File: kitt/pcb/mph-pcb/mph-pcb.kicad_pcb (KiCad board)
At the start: 4 copper layers, 280 x 125 mm, 140 parts, among them J1 Screw_Terminal_01x02, J2 Screw_Terminal_01x03, U1 TLC5940NT, U2 TLC5940NT, U3 TLC5940NT, U4 TLC5940NT, U5 TLC5940NT, U6 TLC5940NT, U7 TLC5940NT

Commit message: routed led display chips
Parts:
- moved C4 232.2 mm to (151.1, 136.2)
- moved NT7 213.6 mm to (231.5, 107.5)
- moved NT5 194.1 mm to (222.7, 39.1), turned to 180 degrees
- moved R3 194.0 mm to (74.2, 81.5), turned to 90 degrees
- moved C8 185.1 mm to (190.7, 110.8), turned to 180 degrees
- moved R4 184.9 mm to (136.4, 48.5), turned to 90 degrees
- moved NT6 170.6 mm to (188.3, 107.5)
- moved R7 164.1 mm to (226.1, 110.3), turned to 180 degrees
- moved C5 159.8 mm to (70.3, 81.5), turned to 90 degrees
- moved R34 159.1 mm to (66.0, 71.4), turned to 270 degrees
- moved C9 158.8 mm to (233.9, 110.1), turned to 180 degrees
- moved NT2 155.8 mm to (148.5, 132.4), turned to 270 degrees
- moved R2 150.0 mm to (159.9, 136.2)
- moved R6 143.7 mm to (182.9, 110.3), turned to 180 degrees
- moved C6 139.2 mm to (132.7, 49.1), turned to 90 degrees
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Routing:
- added copper zone on In2.Cu, net GND

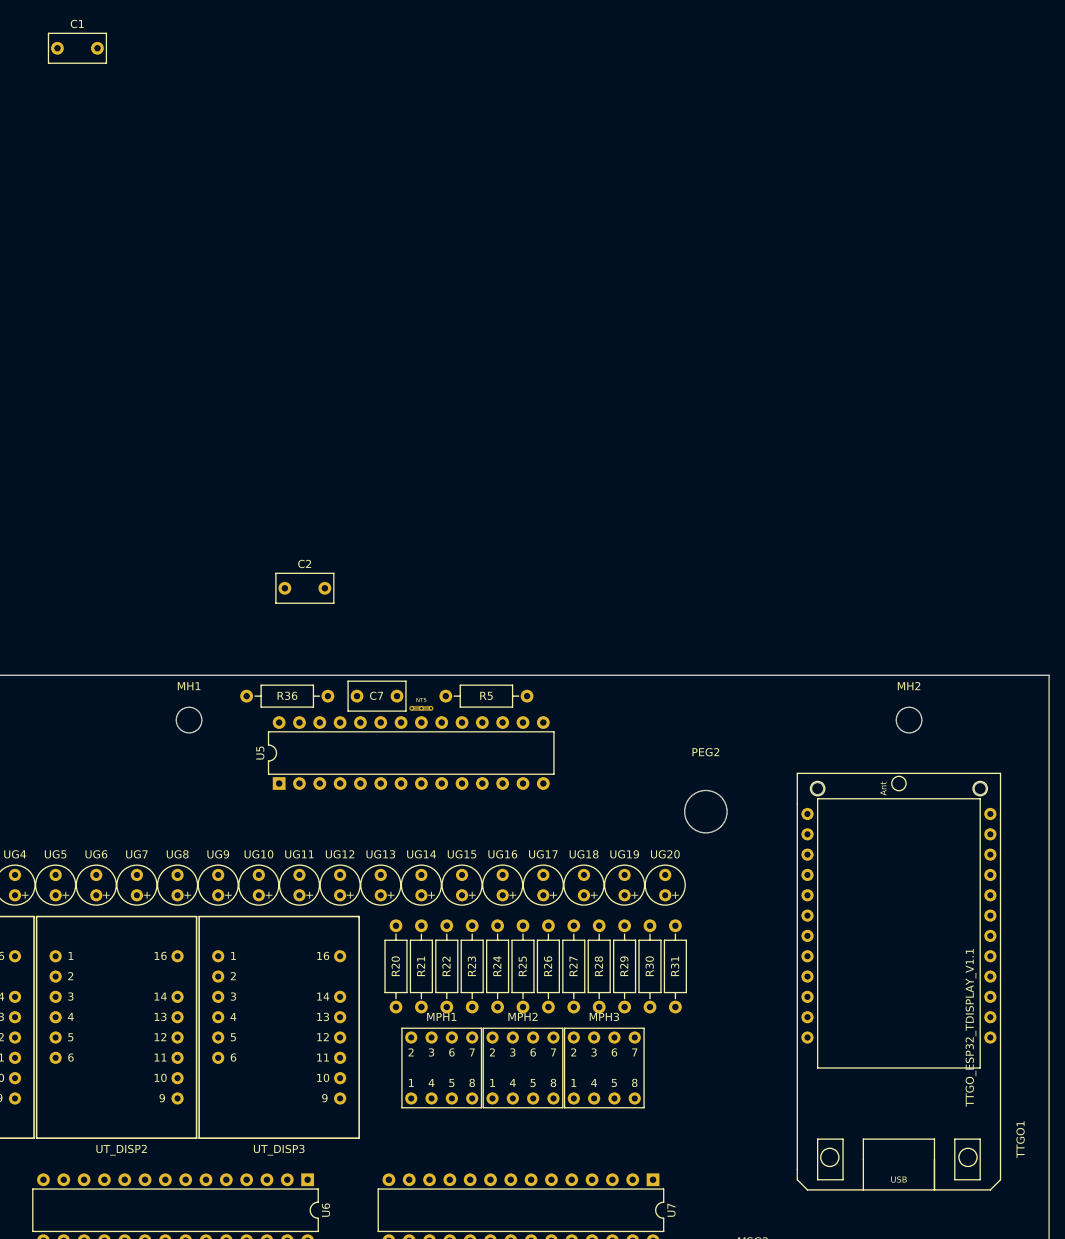
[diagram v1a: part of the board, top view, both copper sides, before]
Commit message: finshed mph placement
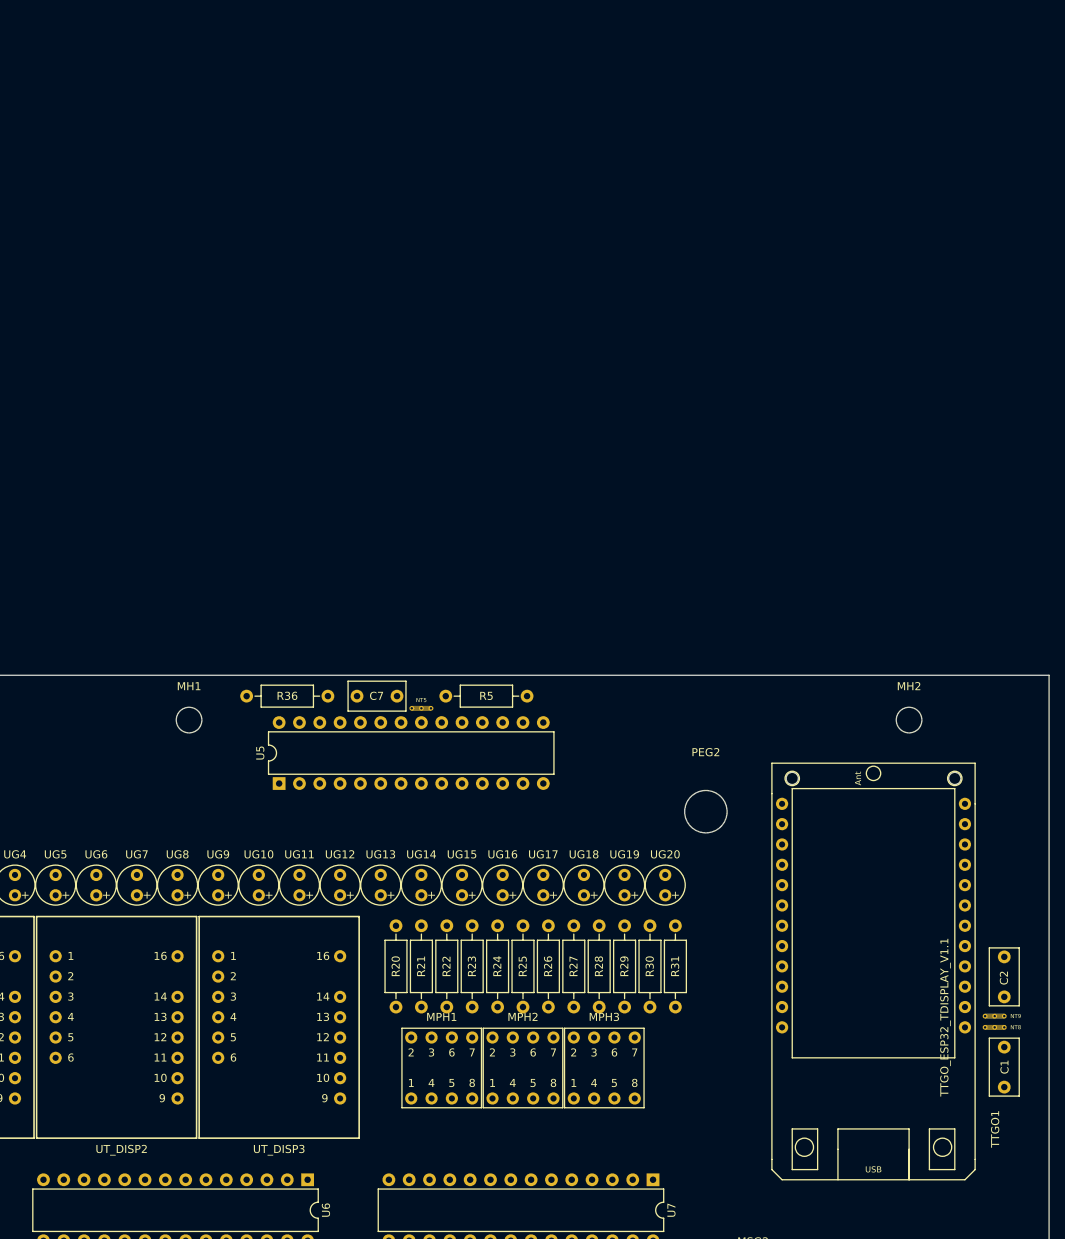
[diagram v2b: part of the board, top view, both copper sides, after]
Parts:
- added NT8: Net-Tie_3_Tee, NetTie:NetTie-3_THT_Pad0.3mm, F.Cu at (292.0, 79.0)
- added NT9: Net-Tie_3_Tee, NetTie:NetTie-3_THT_Pad0.3mm, F.Cu at (294.4, 77.6)
- moved C1 172.0 mm to (294.4, 81.5), turned to 270 degrees
- moved C2 103.4 mm to (294.4, 75.2), turned to 90 degrees
- moved TTGO1 3.42 mm to (290.8, 95.5)
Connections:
- C1 pad 1: +5V -> Net-(C1-Pad1)
- C2 pad 1: +5V -> Net-(C2-Pad1)
- TTGO1 pad 1: +5V -> Net-(NT8-Pad1)

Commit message: fill zones
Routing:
- net Net-(J1-Pad1): track 0.00 -> 15.2 mm
- added copper zone on B.Cu, net GND
- removed copper zone on In2.Cu, net GND

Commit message: more wiring
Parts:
- moved R35 16.1 mm to (114.6, 47.8), turned to 0 degrees
- moved R12 12.7 mm to (96.4, 63.8)
- moved R13 12.7 mm to (93.3, 63.8)
- moved R11 12.7 mm to (99.6, 63.8)
- moved R2 10.5 mm to (151.4, 142.2), turned to 270 degrees
- moved R17 6.35 mm to (102.8, 63.8)
- moved R18 6.35 mm to (106.0, 63.8)
- moved R19 6.35 mm to (109.1, 63.8)
- moved R4 5.84 mm to (136.4, 42.7), turned to 0 degrees
- moved C5 5.26 mm to (74.2, 78.0), turned to 0 degrees
- moved R34 4.98 mm to (70.9, 70.9)
- moved C7 3.97 mm to (221.0, 40.7)
- moved U5 3.97 mm to (206.3, 51.6)
- moved NT5 3.97 mm to (225.3, 42.2)
- moved R36 3.97 mm to (202.2, 40.7)
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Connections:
- TTGO1 pad 3: /BLANK -> /VPRG
- TTGO1 pad 4: /XLAT -> /SCLK
- TTGO1 pad 5: /SCLK -> /XLAT
- TTGO1 pad 7: /VPRG -> /BLANK
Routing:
- net /VPRG: track 0.00 -> 410.8 mm, vias 0 -> 1
- net /SCLK: track 0.00 -> 403.4 mm, vias 0 -> 1
- net /XLAT: track 0.00 -> 401.5 mm, vias 0 -> 1
- net /DCPRG: track 0.00 -> 390.4 mm, vias 0 -> 1
- net /GSCLK: track 0.00 -> 386.8 mm, vias 0 -> 1
- net /BLANK: track 0.00 -> 364.3 mm, vias 0 -> 1
- net /SIG_1: track 0.00 -> 340.2 mm
- net /SIG_2: track 0.00 -> 161.9 mm
- net /LV_TX: track 0.00 -> 151.7 mm
- net /LV_RX: track 0.00 -> 144.8 mm
- net /LV_MSG_TX: track 0.00 -> 134.8 mm
- net /SIG_3: track 0.00 -> 129.4 mm, vias 0 -> 1
- net /MASH_YD3: track 0.00 -> 103.2 mm
- net /MASH_YD1: track 0.00 -> 103.2 mm
- net /MASH_YD2: track 0.00 -> 98.0 mm
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
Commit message: more wiring
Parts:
- removed R33, R34, R35, R36, R37, R38: 10K, Resistor_THT:R_Axial_DIN0207_L6.3mm_D2.5mm_P10.16mm_Horizontal
- MH1, MH2, MH3, MH4, MSG1, MSG2: value MountingHole_3.2mm_M3 -> MountingHole
- PEG1, PEG2, PEG3, PEG4: value MountingHole_5.3mm_M5 -> MountingHole
- THRU1, THRU2: value MountingHole_6.4mm_M6 -> MountingHole
- moved R32 278.7 mm to (293.4, 63.5)
- moved THRU2 6.79 mm to (288.3, 121.9)
- moved THRU1 3.11 mm to (116.8, 152.4)
- moved C7 1.77 mm to (222.2, 39.4)
- moved R7 1.68 mm to (224.8, 109.2)
- moved R5 1.29 mm to (227.1, 39.4)
- moved R6 1.00 mm to (182.9, 111.3)
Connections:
- R32 pad 1: +5V -> /BLANK
- R32 pad 2: /BLANK -> +5V
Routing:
- net /VPRG: track 410.8 -> 608.1 mm
- net /BLANK: track 364.3 -> 444.4 mm
- net /SIG_7: track 0.00 -> 69.3 mm, vias 0 -> 1
- net /DCPRG: track 390.4 -> 441.3 mm, vias 1 -> 2
- net /XLAT: track 401.5 -> 452.1 mm
- net /SCLK: track 403.4 -> 454.0 mm
- net /GSCLK: track 386.8 -> 435.9 mm, vias 1 -> 2
- net /SOUT: track 83.6 -> 75.5 mm, vias 0 -> 2
- net /SIG_1: track 340.2 -> 346.1 mm
- net Net-(R6-Pad1): track 6.26 -> 7.78 mm
- net /UT_DISP2_B: track 74.6 -> 73.2 mm
- net Net-(R5-Pad1): track 3.51 -> 4.80 mm
- net Net-(R7-Pad1): track 6.26 -> 7.36 mm
- net Net-(C7-Pad1): track 2.16 -> 3.07 mm

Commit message: finished wiring mph
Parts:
- moved C5 2.64 mm to (71.6, 78.5)
- moved NT2 1.65 mm to (151.5, 132.5)
- moved R2 1.52 mm to (152.9, 142.2)
- moved C4 1.02 mm to (152.1, 137.9)
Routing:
- net /DCPRG: track 441.3 -> 670.3 mm
- net /SCLK: track 454.0 -> 615.9 mm
- net /XLAT: track 452.1 -> 611.9 mm, vias 1 -> 2
- net /BLANK: track 444.4 -> 599.6 mm, vias 1 -> 2
- net /GSCLK: track 435.9 -> 590.1 mm
- net /VPRG: track 608.1 -> 630.7 mm, vias 1 -> 0
- net /SIG_2: track 161.9 -> 172.0 mm
- net /MASH_DISP1_A: track 40.7 -> 48.8 mm, vias 0 -> 1
- net /UT_DISP1_RDP: track 41.2 -> 36.4 mm
- net /SIG_4: track 69.4 -> 65.0 mm
- net /SOUT: track 75.5 -> 72.2 mm, vias 2 -> 1
- net /MASH_DISP2_F: track 41.9 -> 38.9 mm
- net /MASH_DISP2_A: track 38.1 -> 35.6 mm
- net /UT_DISP2_G: track 68.8 -> 71.2 mm
- net /UT_DISP2_D: track 55.4 -> 57.8 mm
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
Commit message: drc check
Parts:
- moved R32 1.05 mm to (294.4, 63.8)
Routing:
- net /BLANK: track 599.6 -> 600.9 mm

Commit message: fixed pegboard to 25mm spacing
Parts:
- moved PEG1 55.6 mm to (108.0, 53.0)
- moved THRU2 12.1 mm to (286.0, 110.0)
- moved PEG4 11.3 mm to (286.0, 128.0)
- moved PEG2 1.31 mm to (258.0, 53.0)
- moved PEG3 0.66 mm to (58.0, 153.0)
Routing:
- net /GSCLK: track 590.1 -> 589.2 mm
